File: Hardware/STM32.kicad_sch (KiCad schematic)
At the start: 1 part, among them U2 STM32L4R5ZITx

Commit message: Connect RP2040, STM32, temperature sensor
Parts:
- added R1, R2: 4k7, symbol Device:R_US
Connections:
- net SPI2_NCS: now reaches U2.114 (PD0)
- net SPI2_SCK: now reaches U2.115 (PD1)
- net SPI2_MISO: now reaches U2.117 (PD3)
- net SPI2_MOSI: now reaches U2.118 (PD4)
- net I2C4_SCL: now reaches U2.81 (PD12)
- net I2C4_SCL: now also R1.2
- net I2C4_SDA: now reaches U2.82 (PD13)
- net I2C4_SDA: now also R2.2
- new net +3V3: R1.1, R2.1

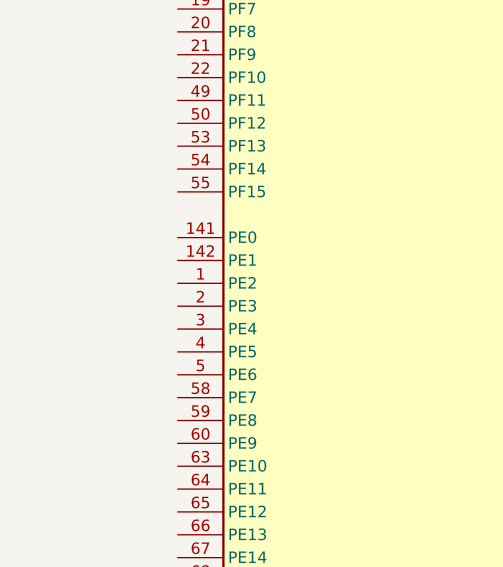
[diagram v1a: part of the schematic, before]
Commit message: Add PC104 header sub-schematic
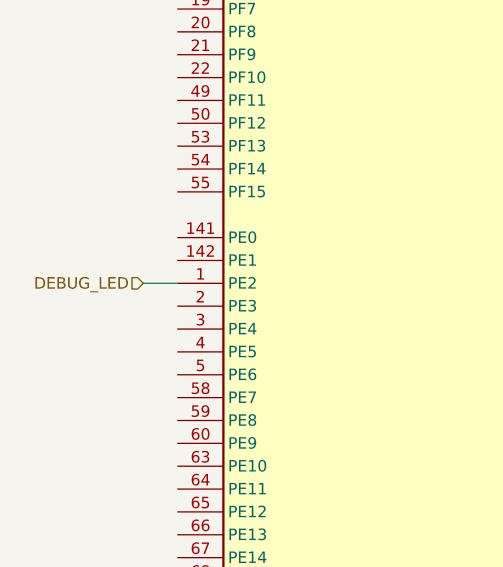
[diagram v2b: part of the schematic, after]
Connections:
- net DEBUG_LED: now reaches U2.1 (PE2)
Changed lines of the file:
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@@
+	(wire
+		(pts
+			(xy 66.04 160.02) (xy 69.85 160.02)
+		)
+		(stroke
+			(width 0)
+			(type default)
+		)
+	)
 	(wire
 		(pts
@@
 		)
 	)
+	(hierarchical_label "DEBUG_LED"
+		(shape input)
+		(at 66.04 160.02 180)
+		(effects
+			(font
+				(size 1.27 1.27)
+			)
+			(justify right)
+		)
+	)

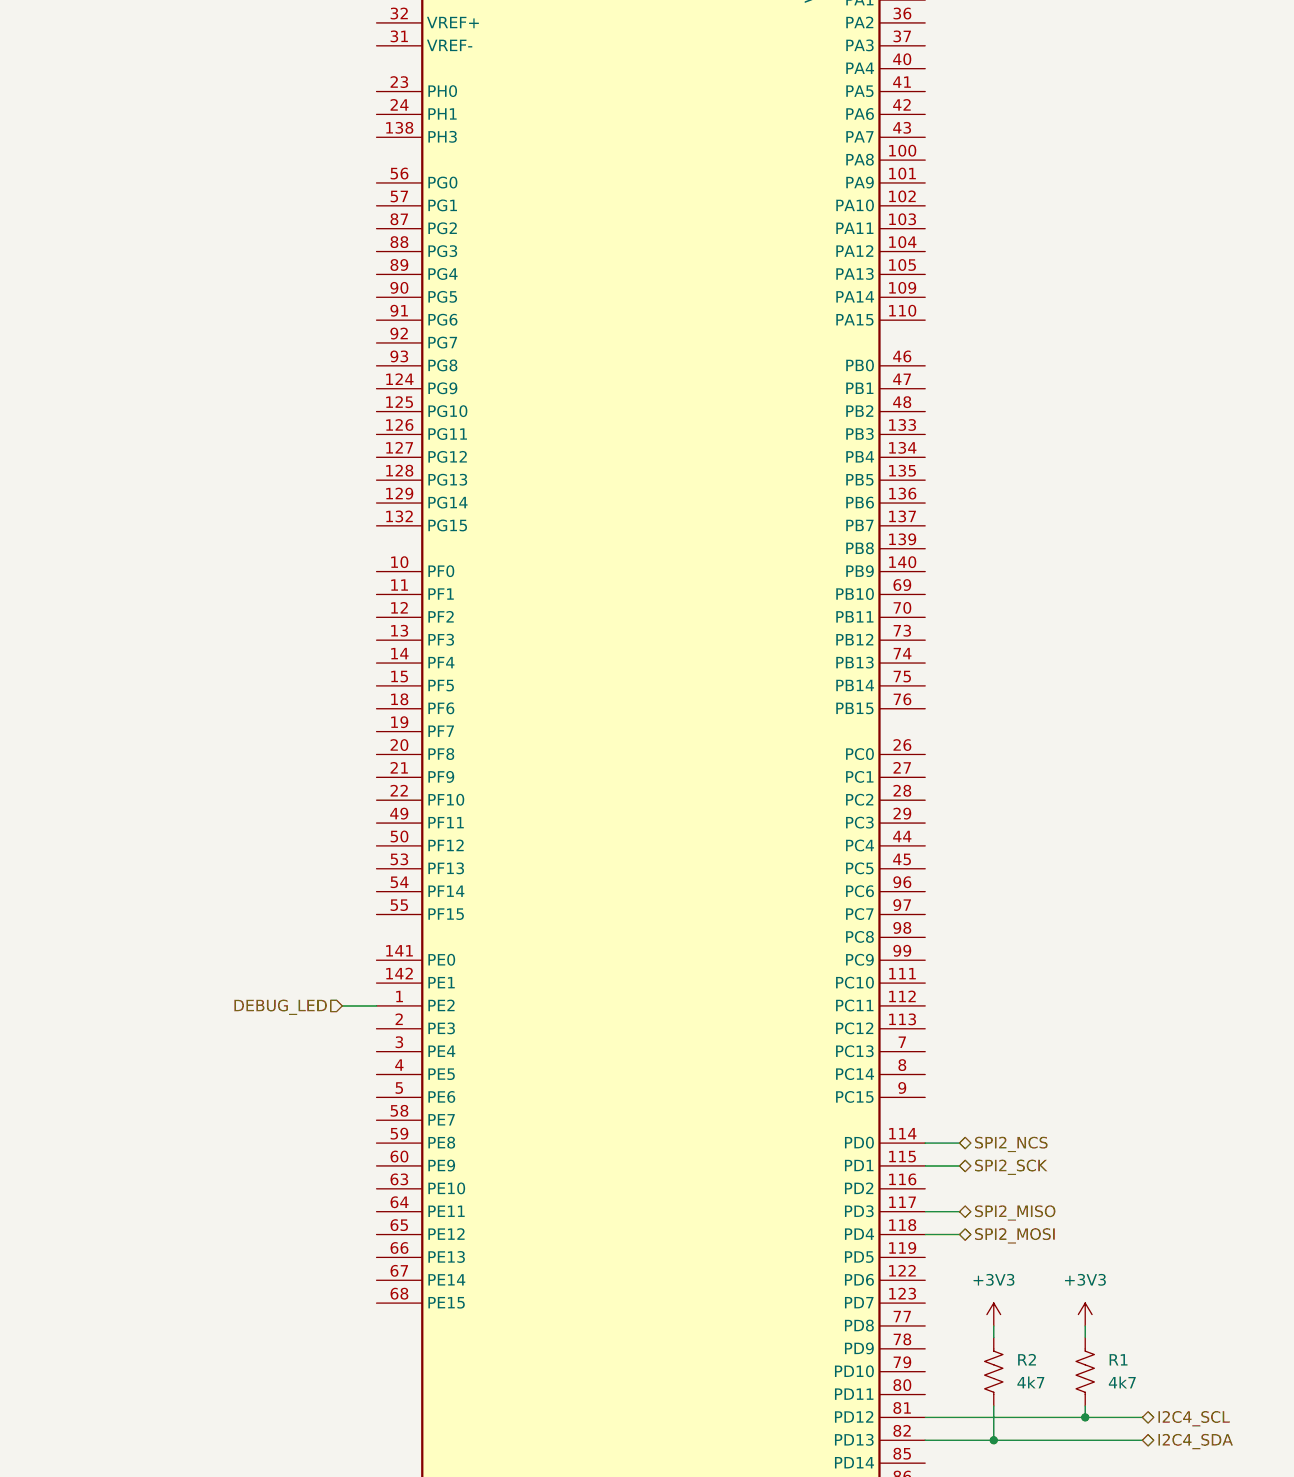
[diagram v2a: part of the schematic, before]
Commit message: Add STM32 I2C and SPI connections
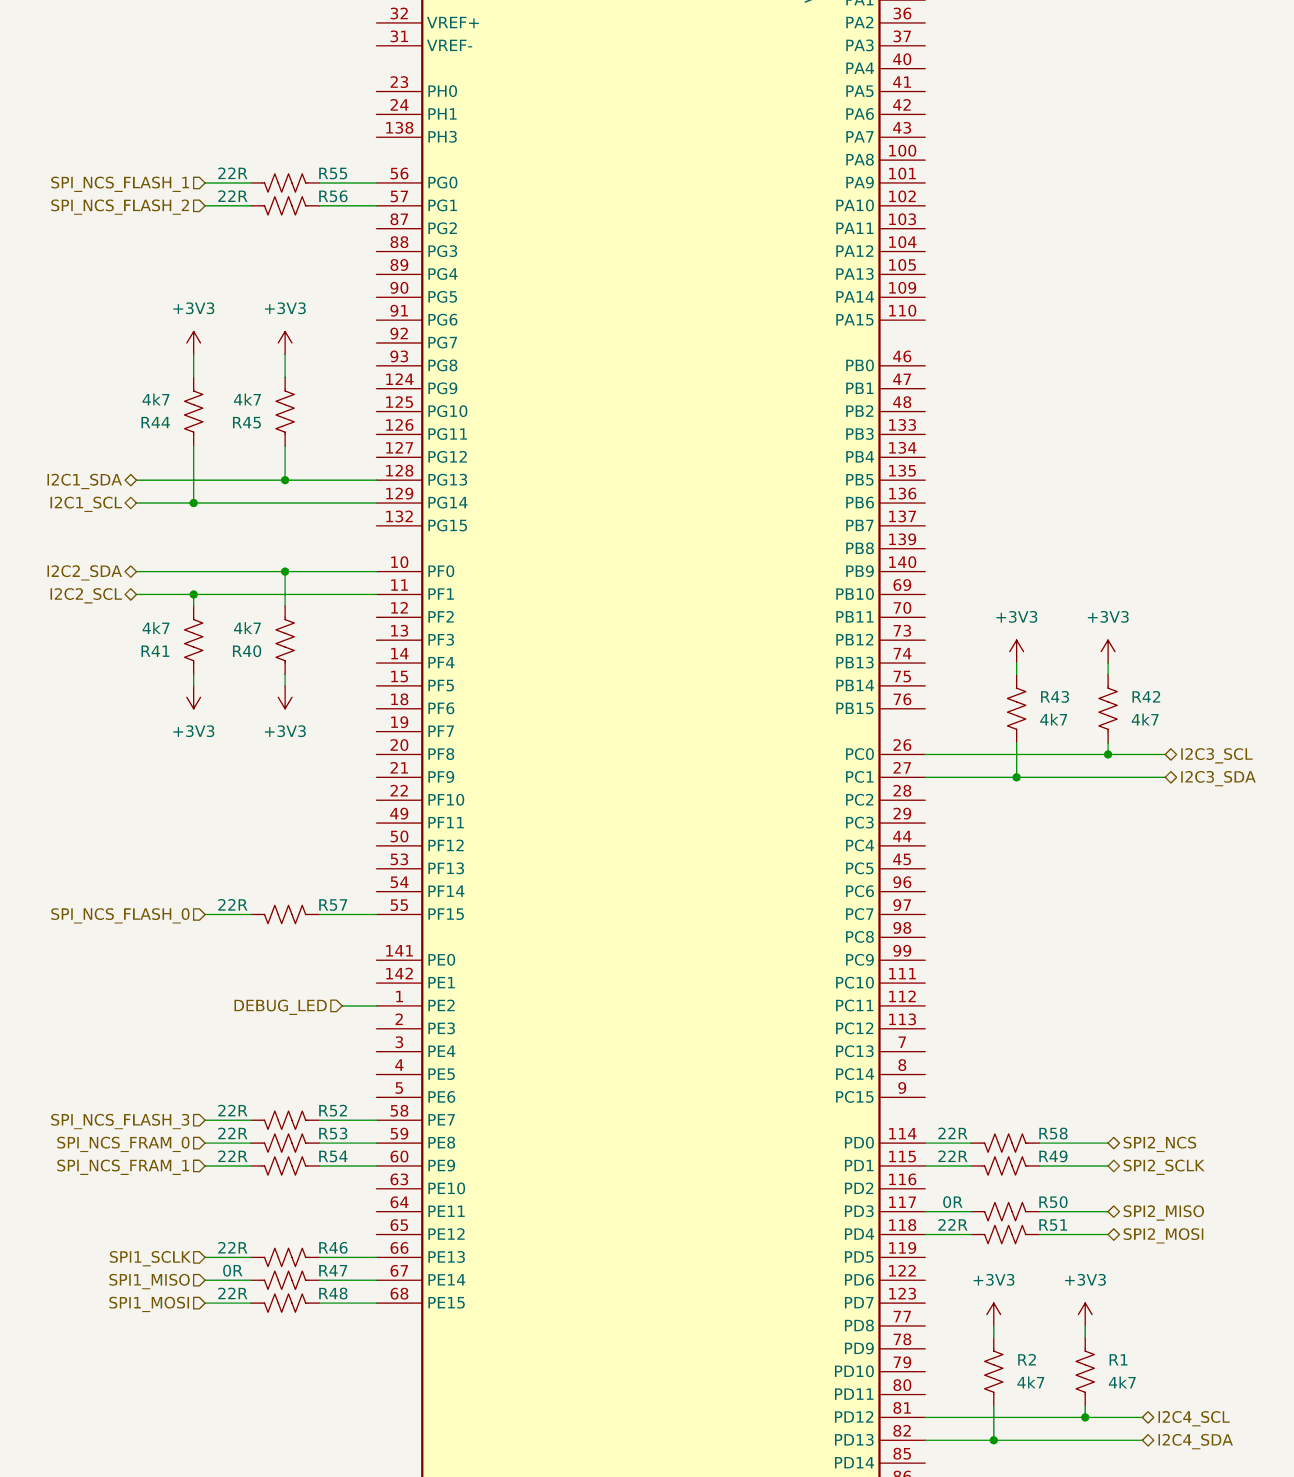
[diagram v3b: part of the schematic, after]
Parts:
- added R40, R41, R42, R43, R44, R45: 4k7, symbol Device:R_US
- added R46, R48, R49, R51, R52, R53, R54, R55, R56, R57, R58: 22R, symbol Device:R_US
- added R47, R50: 0R, symbol Device:R_US
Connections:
- net +3V3: now also R40.1, R41.1, R42.1, R43.1, R44.2, R45.2
- net SPI2_MISO: now also R50.1; no longer U2.117 (PD3)
- net SPI2_MOSI: now also R51.1; no longer U2.118 (PD4)
- net SPI2_NCS: now also R58.1; no longer U2.114 (PD0)
- net I2C2_SDA: now reaches U2.10 (PF0)
- net I2C2_SDA: now also R40.2
- net I2C2_SCL: now reaches U2.11 (PF1)
- net I2C2_SCL: now also R41.2
- net I2C1_SDA: now reaches U2.128 (PG13)
- net I2C1_SDA: now also R45.1
- net I2C1_SCL: now reaches U2.129 (PG14)
- net I2C1_SCL: now also R44.1
- net I2C3_SCL: now reaches U2.26 (PC0)
- net I2C3_SCL: now also R42.2
- net I2C3_SDA: now reaches U2.27 (PC1)
- net I2C3_SDA: now also R43.2
- net at U2.55 (PF15): now also R57.1
- net at U2.56 (PG0): now also R55.1
- net at U2.57 (PG1): now also R56.1
- net at U2.58 (PE7): now also R52.1
- net at U2.59 (PE8): now also R53.1
- net at U2.60 (PE9): now also R54.1
- net at U2.66 (PE13): now also R46.1
- net at U2.67 (PE14): now also R47.1
- net at U2.68 (PE15): now also R48.1
- net SPI2_SCK: no longer names the net of U2.115 (PD1)
- net SPI2_SCK: now also R49.2
- new net: R58.2, U2.114 (PD0)
- new net: R50.2, U2.117 (PD3)
- new net: R51.2, U2.118 (PD4)
- new net SPI1_MISO: R47.2
- new net SPI1_MOSI: R48.2
- new net SPI1_SCLK: R46.2
- new net SPI2_SCLK: R49.1
- new net SPI_NCS_FLASH_0: R57.2
- new net SPI_NCS_FLASH_1: R55.2
- new net SPI_NCS_FLASH_2: R56.2
- new net SPI_NCS_FLASH_3: R52.2
- new net SPI_NCS_FRAM_0: R53.2
- new net SPI_NCS_FRAM_1: R54.2

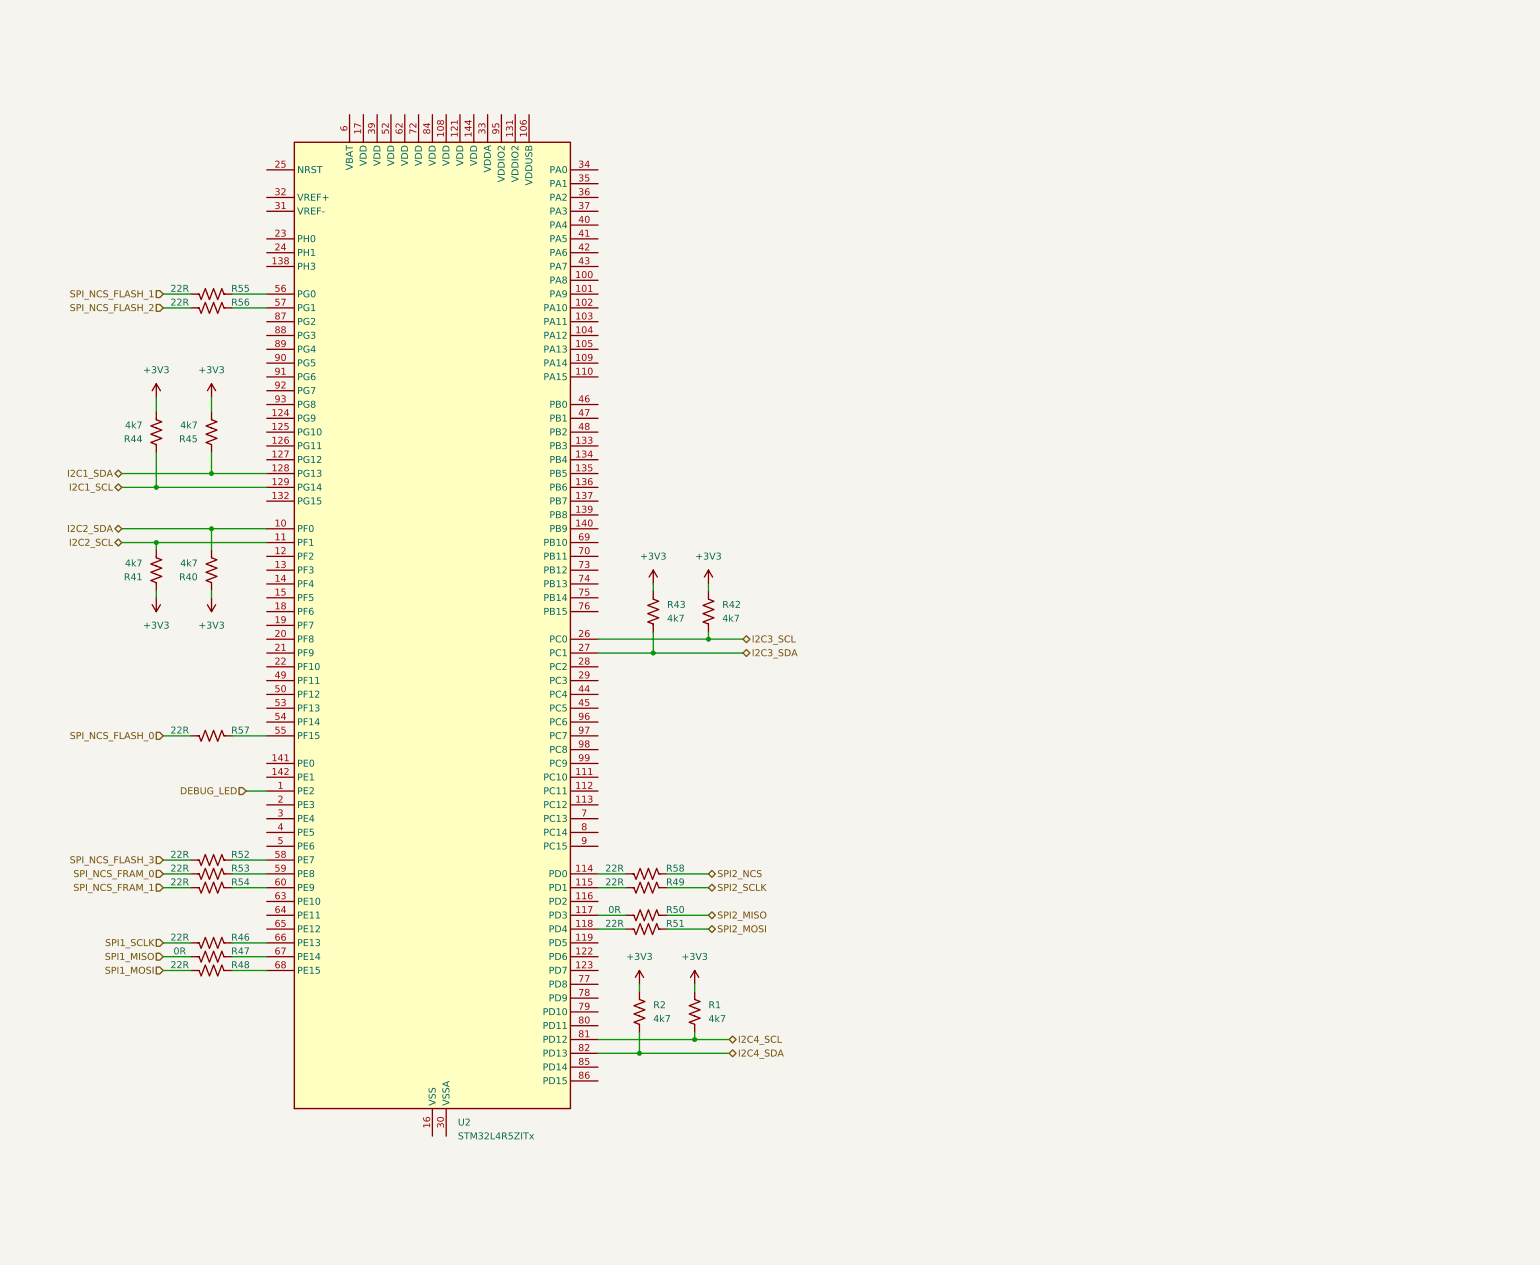
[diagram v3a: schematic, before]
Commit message: Add UARTs to STM32
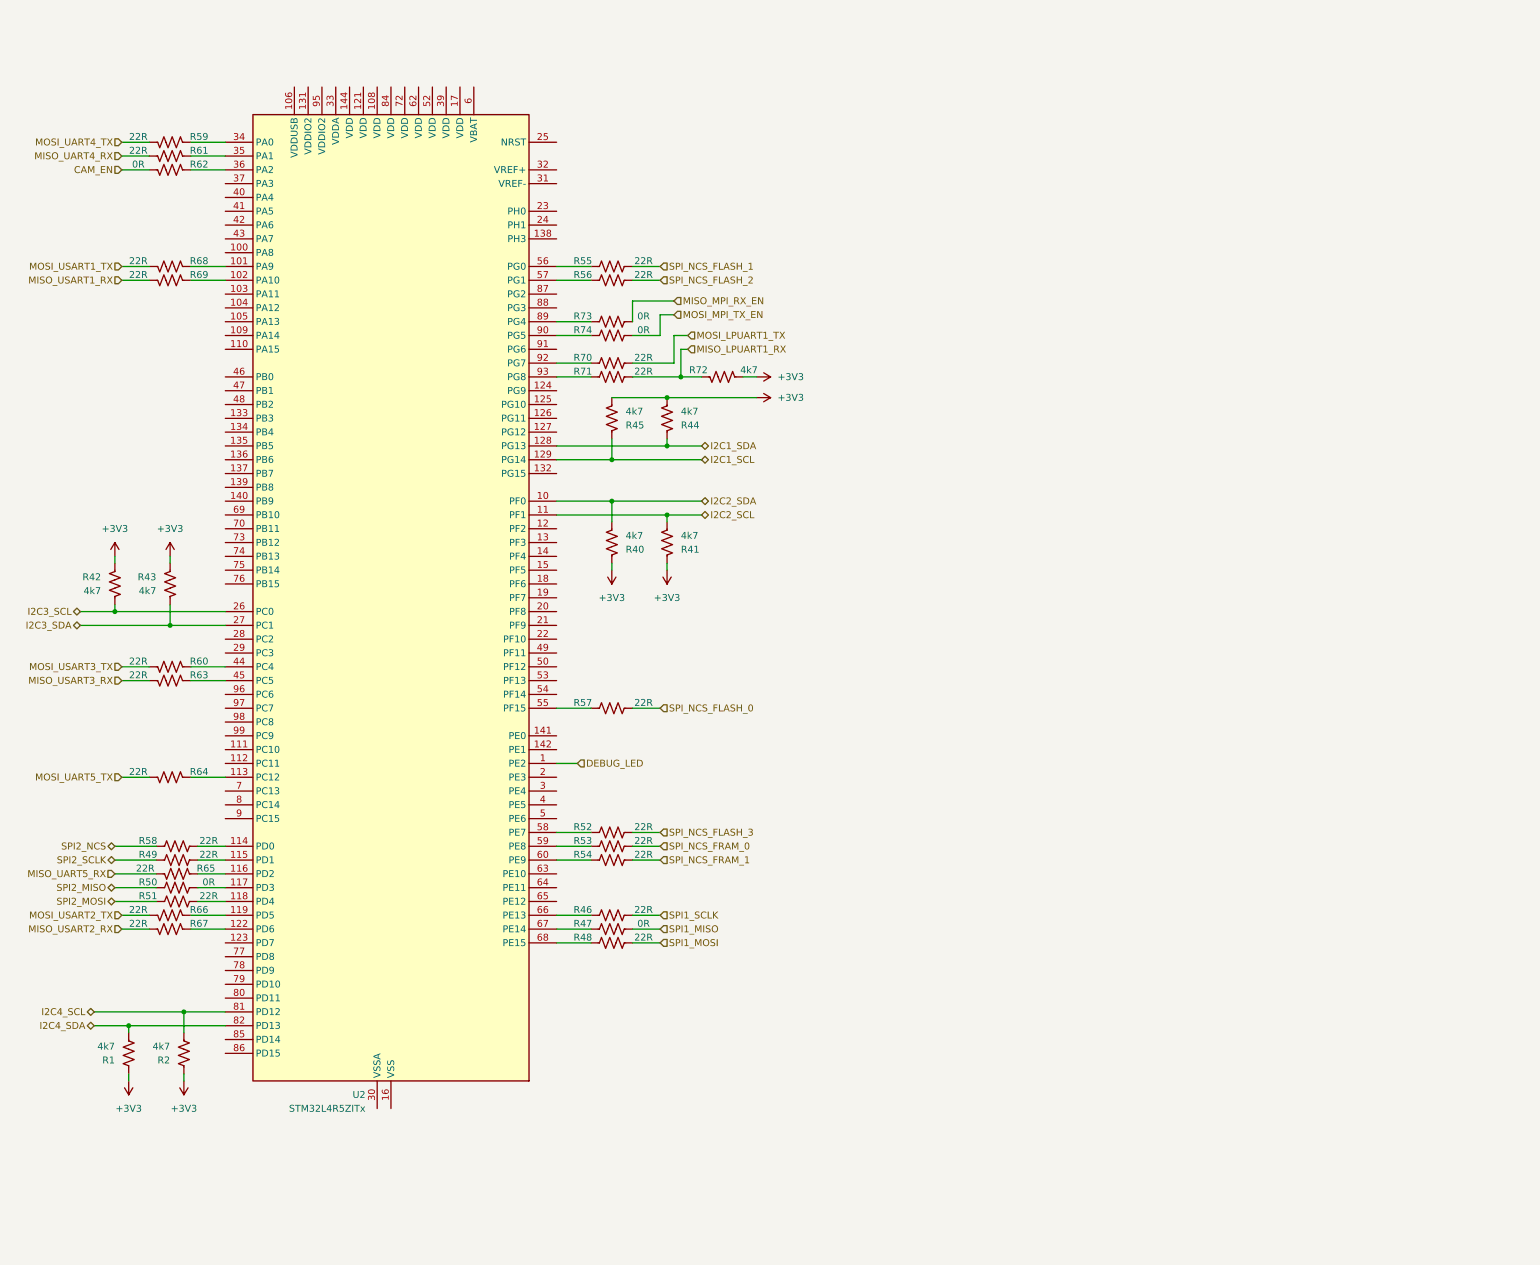
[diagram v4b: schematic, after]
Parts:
- added R59, R60, R61, R63, R64, R65, R66, R67, R68, R69, R70, R71: 22R, symbol Device:R_US
- added R62, R73, R74: 0R, symbol Device:R_US
- added R72: 4k7, symbol Device:R_US
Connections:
- net +3V3: now also R72.1
- net I2C1_SCL: now also R45.1; no longer R44.1
- net I2C1_SDA: now also R44.1; no longer R45.1
- net I2C4_SCL: now also R2.2; no longer R1.2
- net I2C4_SDA: now also R1.2; no longer R2.2
- net at U2.101 (PA9): now also R68.1
- net at U2.102 (PA10): now also R69.1
- net at U2.113 (PC12): now also R64.1
- net at U2.116 (PD2): now also R65.1
- net at U2.119 (PD5): now also R66.1
- net at U2.122 (PD6): now also R67.1
- net at U2.34 (PA0): now also R59.1
- net at U2.35 (PA1): now also R61.1
- net at U2.36 (PA2): now also R62.1
- net at U2.44 (PC4): now also R60.1
- net at U2.45 (PC5): now also R63.1
- net at U2.89 (PG4): now also R73.1
- net at U2.90 (PG5): now also R74.1
- net at U2.92 (PG7): now also R70.1
- net at U2.93 (PG8): now also R71.1
- new net CAM_EN: R62.2
- new net MISO_LPUART1_RX: R71.2, R72.2
- new net MISO_MPI_RX_EN: R73.2
- new net MISO_UART4_RX: R61.2
- new net MISO_UART5_RX: R65.2
- new net MISO_USART1_RX: R69.2
- new net MISO_USART2_RX: R67.2
- new net MISO_USART3_RX: R63.2
- new net MOSI_LPUART1_TX: R70.2
- new net MOSI_MPI_TX_EN: R74.2
- new net MOSI_UART4_TX: R59.2
- new net MOSI_UART5_TX: R64.2
- new net MOSI_USART1_TX: R68.2
- new net MOSI_USART2_TX: R66.2
- new net MOSI_USART3_TX: R60.2
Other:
- moved on the sheet: R1, R2, R40, R41, R42, R43, R44, R45, R46, R47, R48, R49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
